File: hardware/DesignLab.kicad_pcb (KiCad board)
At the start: 2 copper layers, 169.9 x 180.3 mm, 87 parts, among them J1 Micro_SD_Card_Det, J2 Conn_01x04_Female, P1 USB_C_Plug_USB2.0, Q1 DMG3415U-7, SW1 SW_DPDT_x2, SW10 Button, SW11 Button, SW12 RESET, SW13 ON, SW14 VOL, SW15 BOOT, SW2 SW_DPDT_x2, SW3 REC, SW4 Button, SW5 Button, SW6 Button, SW7 Button, SW8 Button, SW9 Button, U1 SPH0641LM4H, U10 MCP4018-xxxxLT, U2 RP2040, U3 QRE1113, U4 QRE1113, U5 QRE1113, U6 AT25SF128A, U7 PAM8302AAD, U8 AP2112K-3.3, U9 QRE1113, Y1 12Mhz

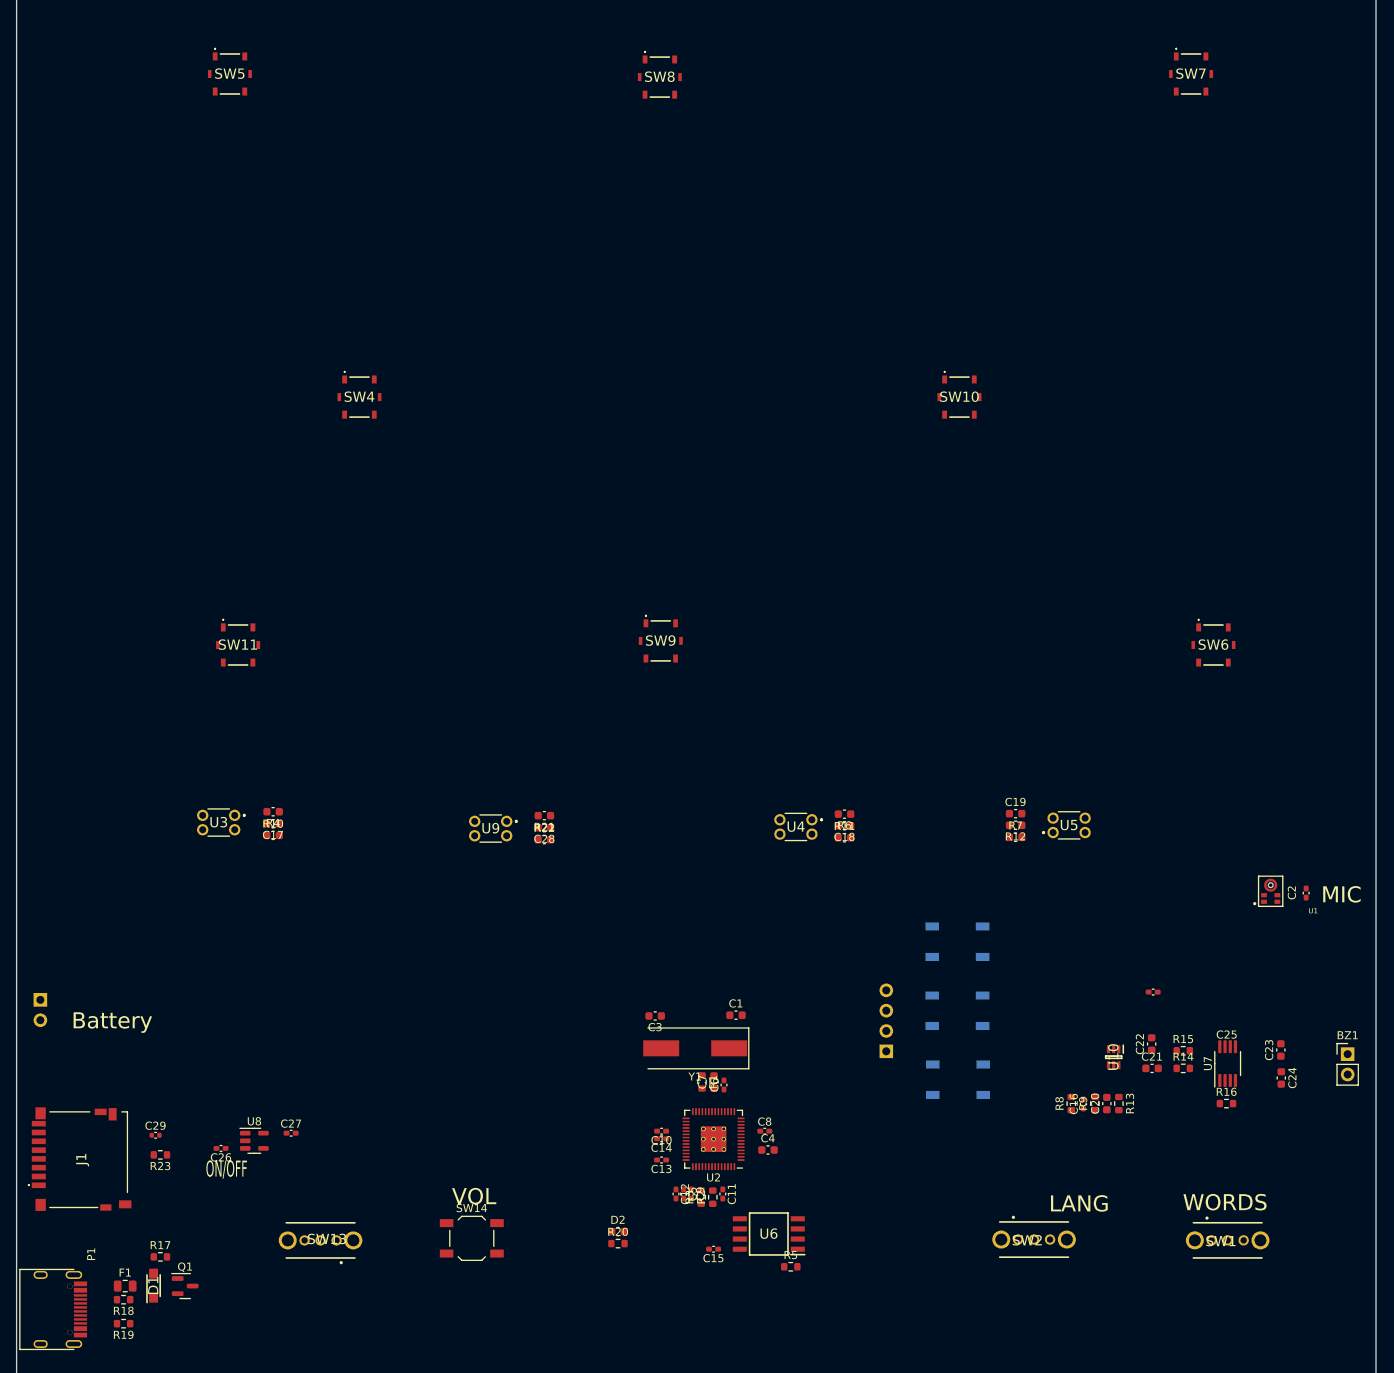
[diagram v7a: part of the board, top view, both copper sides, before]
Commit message: Started routing and BOM corrected
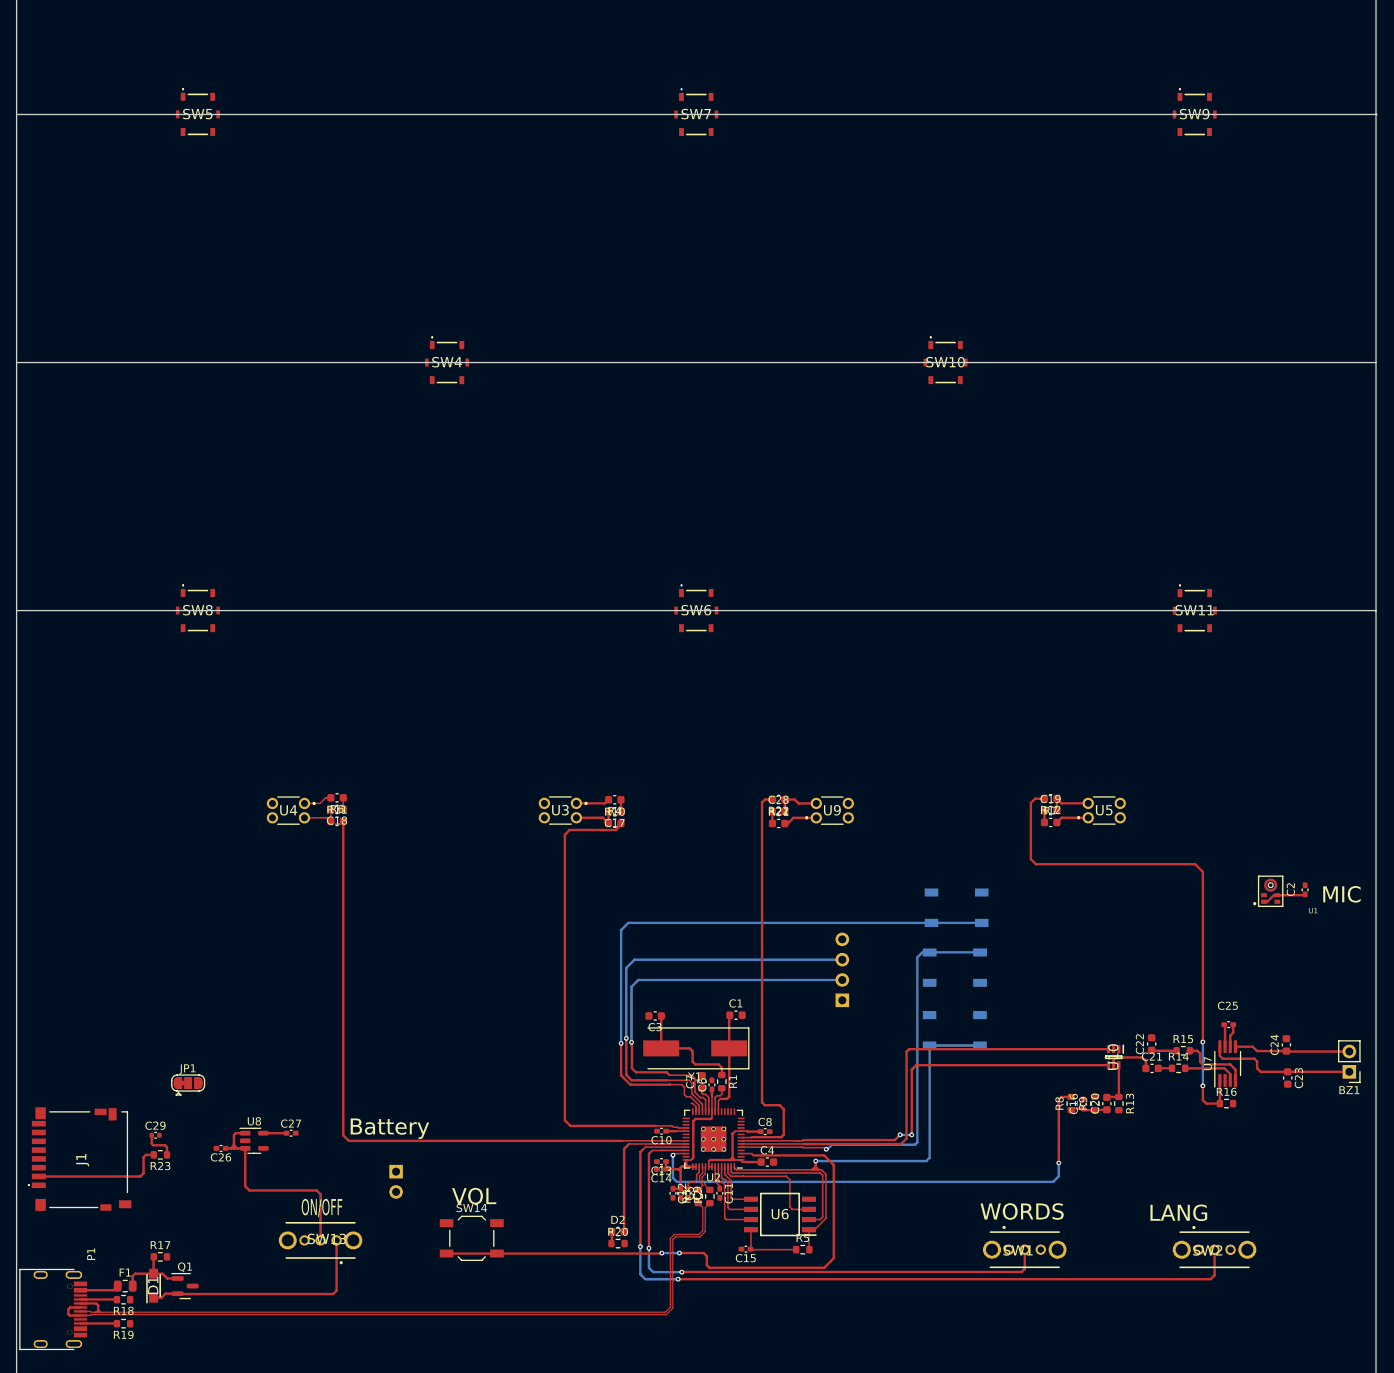
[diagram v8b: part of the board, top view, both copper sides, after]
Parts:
- added JP1: Jumper_3_Bridged12, Jumper:SolderJumper-3_P1.3mm_Bridged12_RoundedPad1.0x1.5mm, F.Cu at (140.6, 173.1)
- moved SW11 119.7 mm to (266.4, 114.1)
- moved SW9 93.7 mm to (266.4, 52.0)
- moved SW8 88.2 mm to (141.8, 114.1)
- moved SW6 64.8 mm to (204.1, 114.1)
- moved C18 63.5 mm to (159.2, 138.9)
- moved R11 63.5 mm to (159.2, 140.4)
- moved R6 63.5 mm to (159.2, 137.5)
- moved U4 63.5 mm to (155.1, 138.2)
- moved SW7 62.1 mm to (204.1, 52.0)
- moved BT4 49.4 mm to (166.6, 184.2)
- moved C17 42.7 mm to (193.9, 139.2)
- moved R10 42.7 mm to (193.9, 140.7)
- moved R4 42.7 mm to (193.9, 137.7)
- moved U3 42.7 mm to (189.1, 138.2)
- moved U9 38.7 mm to (219.1, 140.0), turned to 0 degrees
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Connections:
- J1 pad 10: /CD -> GND
- J1 pad 12: (no net) -> GND
- SW10 pad A1: (no net) -> GND
- SW10 pad A2: (no net) -> GND
- SW10 pad B1: (no net) -> /D6
- SW10 pad B2: (no net) -> /D6
- SW10 pad C1: (no net) -> GND
- SW10 pad C2: (no net) -> GND
- SW11 pad A1: (no net) -> GND
- SW11 pad A2: (no net) -> GND
- SW11 pad B1: (no net) -> /D4
- SW11 pad B2: (no net) -> /D4
- SW11 pad C1: (no net) -> GND
- SW11 pad C2: (no net) -> GND
- SW4 pad A1: (no net) -> GND
- SW4 pad A2: (no net) -> GND
- SW4 pad B1: (no net) -> /D3
- SW4 pad B2: (no net) -> /D3
- SW4 pad C1: (no net) -> GND
- SW4 pad C2: (no net) -> GND
- SW5 pad A1: (no net) -> GND
- SW5 pad A2: (no net) -> GND
- SW5 pad B1: (no net) -> /D2
- SW5 pad B2: (no net) -> /D2
- SW5 pad C1: (no net) -> GND
- SW5 pad C2: (no net) -> GND
- SW6 pad A1: (no net) -> GND
- SW6 pad A2: (no net) -> GND
- SW6 pad B1: (no net) -> /D0
- SW6 pad B2: (no net) -> /D0
- SW6 pad C1: (no net) -> GND
- SW6 pad C2: (no net) -> GND
- SW7 pad A1: (no net) -> GND
- SW7 pad A2: (no net) -> GND
- SW7 pad B1: (no net) -> /D1
- SW7 pad B2: (no net) -> /D1
- SW7 pad C1: (no net) -> GND
- SW7 pad C2: (no net) -> GND
- SW8 pad A1: (no net) -> GND
- SW8 pad A2: (no net) -> GND
- SW8 pad B1: (no net) -> /D7
- SW8 pad B2: (no net) -> /D7
- SW8 pad C1: (no net) -> GND
- SW8 pad C2: (no net) -> GND
- SW9 pad A1: (no net) -> GND
- SW9 pad A2: (no net) -> GND
- SW9 pad B1: (no net) -> /D5
- SW9 pad B2: (no net) -> /D5
- SW9 pad C1: (no net) -> GND
- SW9 pad C2: (no net) -> GND
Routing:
- net /LANG: track 0.00 -> 96.6 mm, vias 0 -> 2
- net /D+: track 0.00 -> 95.1 mm
- net /D-: track 0.00 -> 94.8 mm
- net /S2: track 0.00 -> 82.4 mm
- net /RST: track 0.00 -> 76.3 mm, vias 0 -> 1
- net /VOL: track 0.00 -> 74.2 mm, vias 0 -> 2
- net /WORD: track 0.00 -> 68.8 mm, vias 0 -> 2
- net +3V3: track 0.00 -> 67.1 mm
- net /S1: track 0.00 -> 64.8 mm, vias 0 -> 2
- net /A2: track 0.00 -> 64.6 mm, vias 0 -> 2
- net /QSPI_CS: track 0.00 -> 59.5 mm, vias 0 -> 1
- net /S3: track 0.00 -> 59.0 mm
- net /SDA: track 0.00 -> 57.4 mm
- net /SCL: track 0.00 -> 54.6 mm, vias 0 -> 2
- net /REC: track 0.00 -> 53.7 mm, vias 0 -> 1
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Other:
- board size 169.9 x 180.3 mm -> 170.1 x 180.3 mm
